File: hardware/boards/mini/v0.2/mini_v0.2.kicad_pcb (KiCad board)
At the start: 8 copper layers, 20 x 41 mm, 99 parts, among them IC1 NAU88C22YG, IC3 IS42S16160J-6BLI, J2 Top, J3 Bottom, Q1 PMV37EN22, U1 W25Q128JVP, U2 LTV-217-G, U4 STM32H750XBHx, Y1 Crystal_GND24, Y3 32.768kHz

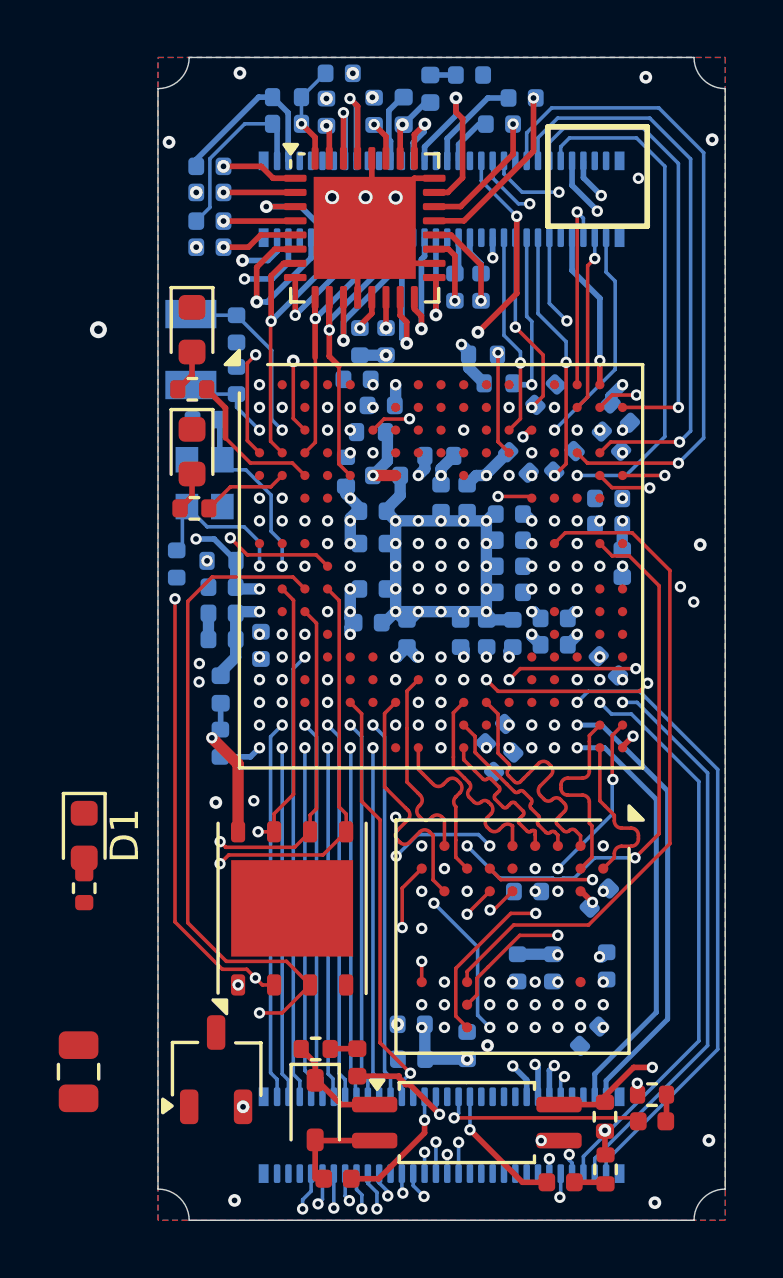
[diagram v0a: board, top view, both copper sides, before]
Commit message: mini: various routing cleanup
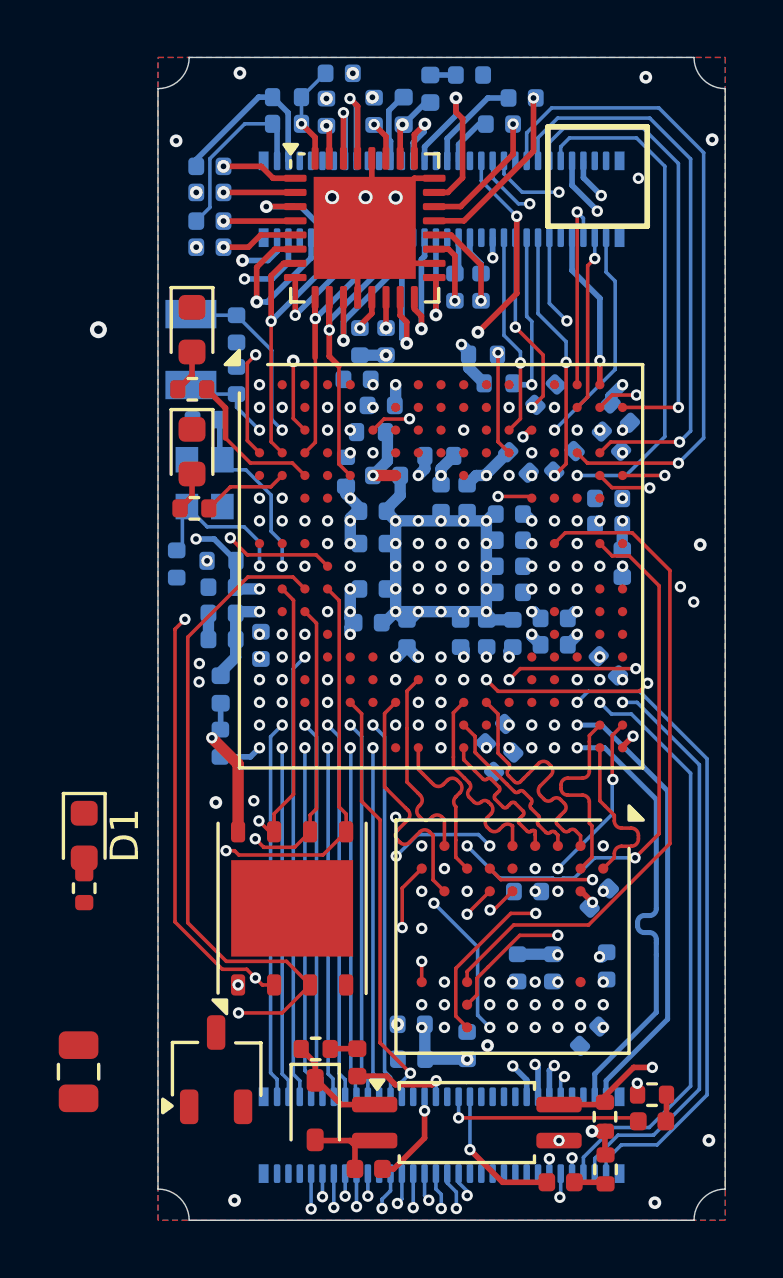
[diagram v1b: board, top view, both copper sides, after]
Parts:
- moved FB3 1.15 mm to (77.4, 96.2)
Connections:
- J3 pad 28: /PA0 -> /EXT_QSPI_DETECT
- J3 pad 30: /PC3 -> /QSPI_CS_EXP
- J3 pad 32: /PC2_C -> /QSPI_CLK
- J3 pad 34: /PH3 -> /QSPI_IO0
- J3 pad 36: /PC1 -> /QSPI_IO1
- J3 pad 38: /PC2 -> /QSPI_IO2
- J3 pad 40: unconnected-(J3-Pad40) -> /QSPI_IO3
- J3 pad 42: /EXT_QSPI_DETECT -> unconnected-(J3-Pad42)
- J3 pad 44: /QSPI_CS_EXP -> /PA0
- J3 pad 46: /QSPI_IO3 -> /PC3
- J3 pad 48: /QSPI_IO2 -> /PC2_C
- J3 pad 50: /QSPI_IO1 -> /PH3
- J3 pad 52: /QSPI_IO0 -> /PC1
- J3 pad 54: /QSPI_CLK -> /PC2
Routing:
- net /QSPI_IO2: track 32.4 -> 38.2 mm
- net /PC1: track 29.3 -> 24.4 mm
- net /QSPI_IO1: track 31.9 -> 36.4 mm
- net /PC3: track 18.9 -> 23.2 mm
- net /PH3: track 21.0 -> 24.8 mm
- net /PC2: track 30.4 -> 26.9 mm
- net /PC2_C: track 19.1 -> 22.5 mm
- net /PA0: track 17.7 -> 20.9 mm
- net /QSPI_CS_EXP: track 38.7 -> 35.9 mm
- net /EXT_QSPI_DETECT: track 37.6 -> 34.9 mm
- net /QSPI_IO3: track 25.8 -> 28.3 mm
- net /QSPI_IO0: track 28.3 -> 29.8 mm
- net /USB_D-: track 14.9 -> 15.8 mm
- net /DIN_IN_SINK: track 4.23 -> 3.39 mm
- net /DIN_IN_SOURCE: track 4.16 -> 3.53 mm
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
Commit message: mini: add license identifier to silkscreen
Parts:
- added REF**: OSHW-Logo2_7.3x6mm_SilkScreen, Symbol:OSHW-Logo2_7.3x6mm_SilkScreen, B.Cu at (76.8, 82.2)
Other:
- board text added: "CERN-OHL-S-2.0"

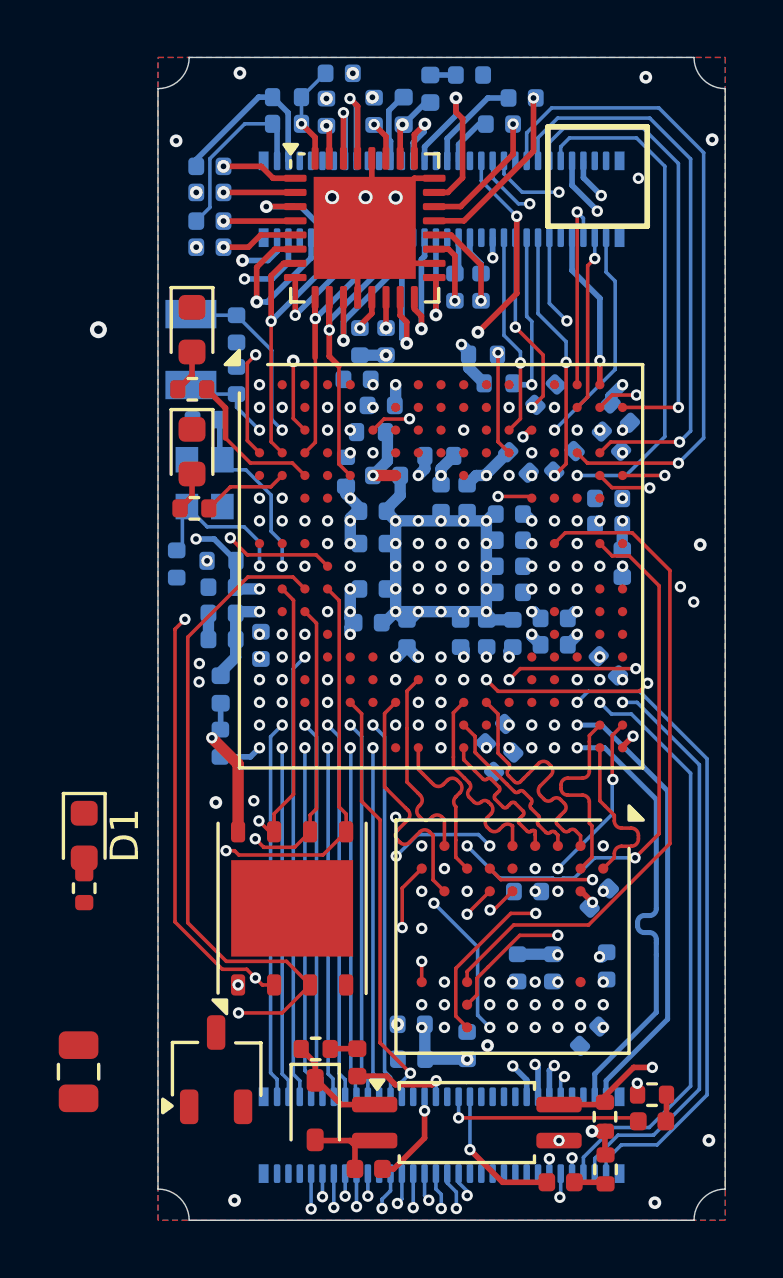
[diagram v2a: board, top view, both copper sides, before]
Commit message: mini: route power supply protections
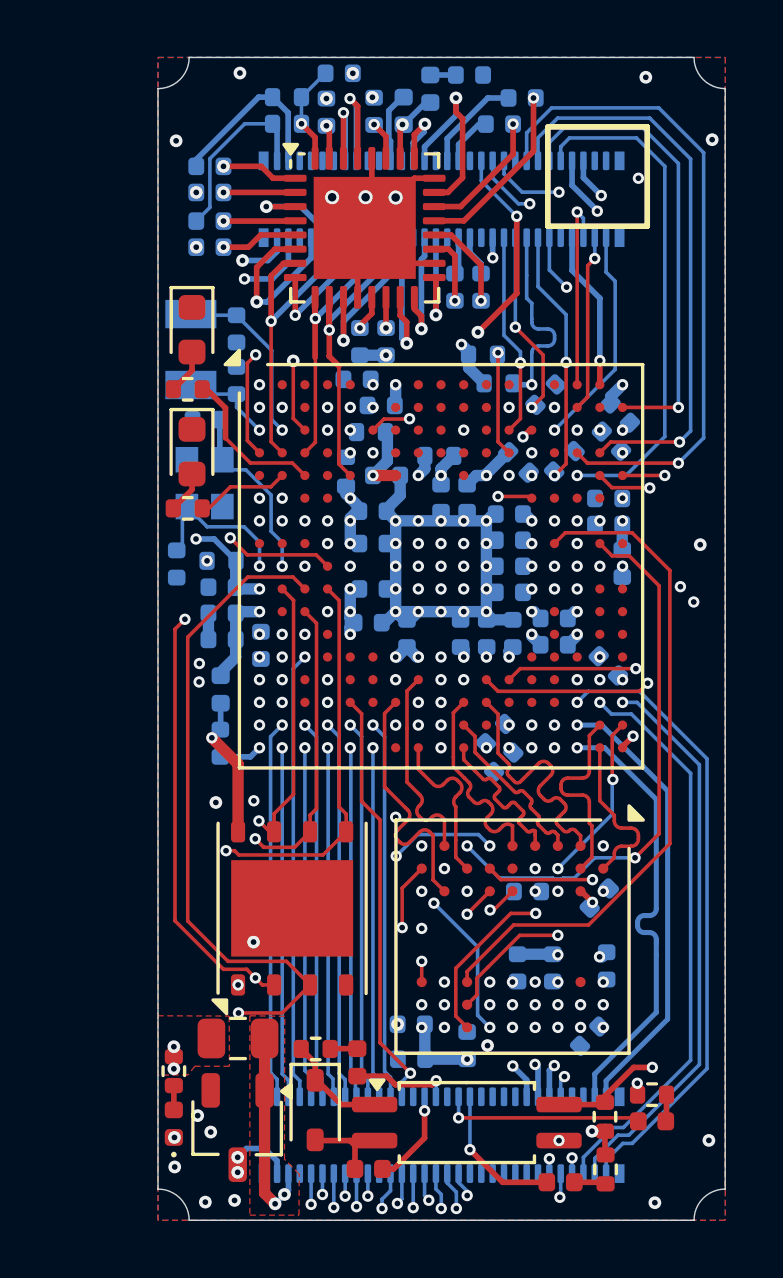
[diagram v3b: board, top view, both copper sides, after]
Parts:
- D1: footprint LED_SMD:LED_0603_1608Metric -> LED_SMD:LED_0402_1005Metric
- moved D1 10.6 mm to (70.6, 94.6), turned to 90 degrees
- moved REF** 9.73 mm to (86.5, 82.7), turned to -90 degrees
- moved R16 7.18 mm to (70.6, 92.7), turned to -90 degrees
- moved F1 5.74 mm to (72.8, 91.6), turned to 0 degrees
- moved Q1 2.18 mm to (72.8, 94.7), turned to -90 degrees
- moved R17 0.23 mm to (71.0, 72.9)
- moved R15 0.16 mm to (71.0, 68.7)
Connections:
- net /3v3+ renamed /VIN
- net /3v3_GND renamed /VIN_GND
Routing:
- net /VIN: track 0.00 -> 7.24 mm, vias 0 -> 2
- net /VIN_GND: track 0.00 -> 2.68 mm, vias 0 -> 2
- net unconnected-(U4H-PH15-PadB16): track 1.47 -> 0.00 mm, vias 1 -> 0
- net /SDMMC1_D2: track 5.94 -> 7.10 mm
- net /FMC_BA1: track 21.5 -> 20.5 mm
- net /PD11: track 22.6 -> 22.0 mm
- net /PD12: track 20.7 -> 20.1 mm
- net /PD13: track 20.3 -> 19.8 mm
- net GND: vias 80 -> 85
- net /DIN_MIDI_TX: vias 3 -> 2
- net /DIN_MIDI_RX: vias 3 -> 2
- net +3.3V: vias 41 -> 43
- added copper zone on F.Cu, net +3.3V
- added copper zone on F.Cu, net /VIN
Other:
- board text added: "@northernpaws"
